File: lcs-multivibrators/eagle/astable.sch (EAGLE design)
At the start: 10 parts, among them T1 BC547, T2 BC547

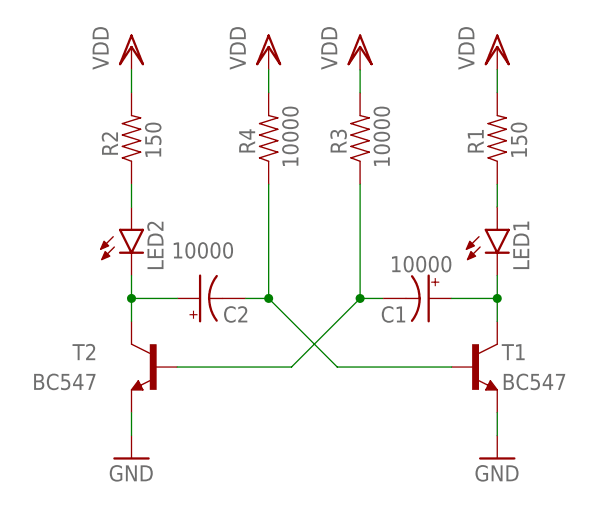
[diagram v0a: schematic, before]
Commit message: multivibrators: fix a few mistakes found during presentation
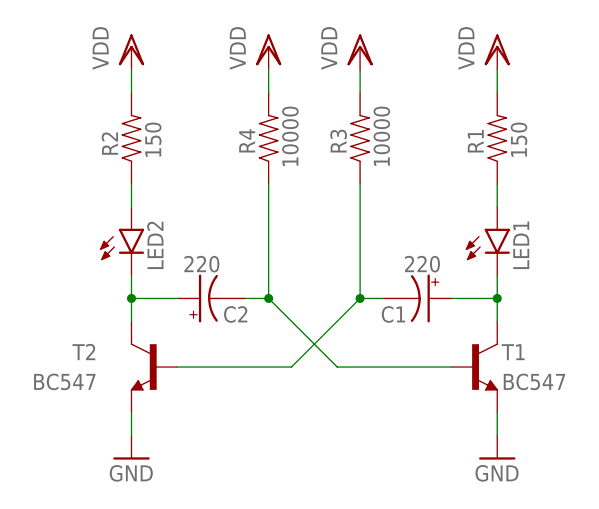
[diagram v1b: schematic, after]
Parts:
- C1, C2: value 10000 -> 220
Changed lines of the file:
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@@
 <part name="R4" library="SparkFun-Passives" deviceset="RESISTOR" device="PTH-1/2W" value="10000"/>
 <part name="VDD3" library="supply1" deviceset="VDD" device=""/>
-<part name="C1" library="SparkFun-Passives" deviceset="CAP_POL" device="PTH4" value="10000"/>
-<part name="C2" library="SparkFun-Passives" deviceset="CAP_POL" device="PTH4" value="10000"/>
+<part name="C1" library="SparkFun-Passives" deviceset="CAP_POL" device="PTH4" value="220"/>
+<part name="C2" library="SparkFun-Passives" deviceset="CAP_POL" device="PTH4" value="220"/>
 <part name="VDD4" library="supply1" deviceset="VDD" device=""/>
 </parts>
@@
 <instance part="C1" gate="G$1" x="27.94" y="60.96" smashed="yes" rot="R270">
 <attribute name="NAME" x="22.606" y="58.293" size="1.778" layer="95"/>
-<attribute name="VALUE" x="23.622" y="63.881" size="1.778" layer="96"/>
+<attribute name="VALUE" x="25.146" y="63.881" size="1.778" layer="96"/>
 </instance>
 <instance part="C2" gate="G$1" x="2.54" y="60.96" smashed="yes" rot="R90">
 <attribute name="NAME" x="5.08" y="58.293" size="1.778" layer="95" rot="R180" align="top-right"/>
-<attribute name="VALUE" x="6.35" y="65.405" size="1.778" layer="96" rot="R180" align="top-left"/>
+<attribute name="VALUE" x="4.826" y="65.659" size="1.778" layer="96" rot="R180"/>
 </instance>
 <instance part="VDD4" gate="G$1" x="10.16" y="88.9"/>
